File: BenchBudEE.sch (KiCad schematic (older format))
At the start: 0 parts

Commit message: Finished Thermocouple Unit
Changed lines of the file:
@@
 Sheet 1 8
 Title ""
-Date "1 feb 2014"
+Date "4 feb 2014"
 Rev ""
 Comp ""
@@
 $EndDescr
 $Sheet
-S 1450 4800 2400 1650
+S 1450 4800 1700 2600
 U 52ED0B6E
 F0 "Arduino" 50
 F1 "Arduino.sch" 50
+F2 "RELAY+" O R 3150 6750 60
+F3 "RELAY -" I R 3150 6950 60
+F4 "MOSI" O R 3150 6000 60
+F5 "MISO" I R 3150 6150 60
+F6 "SCLK" O R 3150 6300 60
+F7 "CS_N" O R 3150 6450 60
+F8 "LED_EN" O R 3150 5600 60
+F9 "LED_FREQ" O R 3150 5750 60
+F10 "FAN_EN" O R 3150 5200 60
+F11 "TACH_MEAS" I R 3150 5400 60
 $EndSheet
 $Sheet
@@
 F2 "TC IN +" I R 10100 4550 60
 F3 "TC IN -" I R 10100 4800 60
+F4 "MOSI" I L 8000 4550 60
+F5 "MISO" O L 8000 4750 60
+F6 "CLK" I L 8000 4950 60
+F7 "CS_N" I L 8000 5100 60
 $EndSheet
 $Sheet
@@
 F0 "Relay" 50
 F1 "Relay.sch" 50
+F2 "DIN+" I L 7950 6250 60
+F3 "DIN-" O L 7950 6500 60
+F4 "RELAY+" I R 10150 6250 60
+F5 "RELAY-" O R 10150 6550 60
 $EndSheet
 $Sheet
@@
 F0 "LED_Driver" 50
 F1 "LED_Driver.sch" 50
-$EndSheet
-$Sheet
-S 8100 900  1800 1250
-U 52ED0CE0
-F0 "Fan" 50
-F1 "Fan.sch" 50
+F2 "EN" I L 8100 2900 60
+F3 "FREQ" I L 8100 3200 60
+F4 "STRING+" O R 9950 2900 60
+F5 "STRING-" I R 9950 3250 60
 $EndSheet
 $Sheet
@@
 F1 "TerminalBlock.sch" 50
 $EndSheet
+$Sheet
+S 8100 900  1800 1250
+U 52ED0CE0
+F0 "Fan" 50
+F1 "Fan.sch" 50
+F2 "Power+" O R 9900 1200 60
+F3 "Power-" I R 9900 1400 60
+F4 "Tach" I R 9900 1600 60
+F5 "Tach_out" O L 8100 1400 60
+F6 "Fan_in" I L 8100 1200 60
+$EndSheet
 $EndSCHEMATC

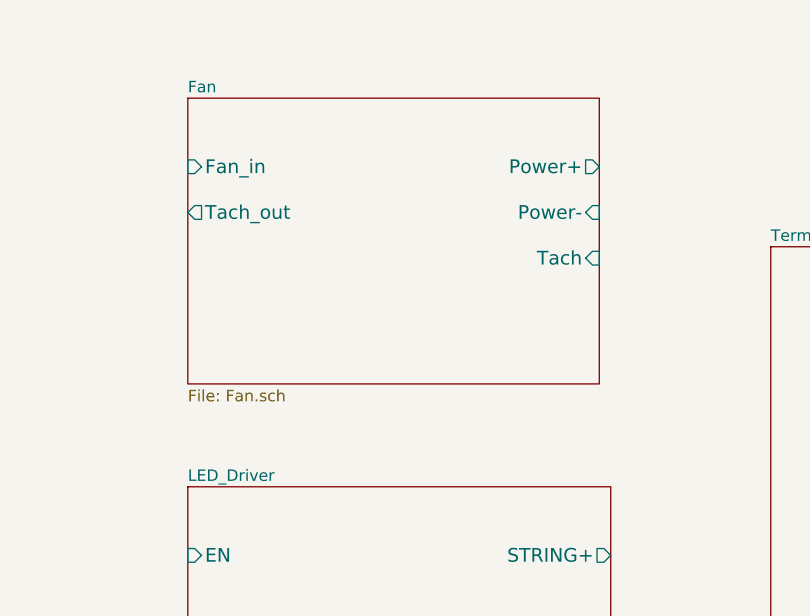
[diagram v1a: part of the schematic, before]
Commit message: After Current/Fan Driver Module
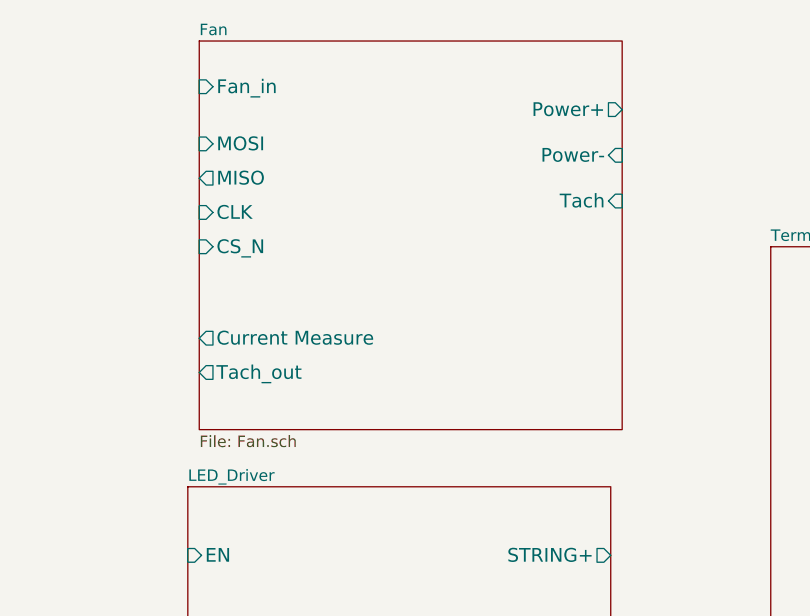
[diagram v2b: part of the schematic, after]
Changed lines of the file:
@@
 $EndSheet
 $Sheet
-S 8100 900  1800 1250
+S 8150 650  1850 1700
 U 52ED0CE0
 F0 "Fan" 50
 F1 "Fan.sch" 50
-F2 "Power+" O R 9900 1200 60
-F3 "Power-" I R 9900 1400 60
-F4 "Tach" I R 9900 1600 60
-F5 "Tach_out" O L 8100 1400 60
-F6 "Fan_in" I L 8100 1200 60
+F2 "Power+" O R 10000 950 60
+F3 "Power-" I R 10000 1150 60
+F4 "Tach" I R 10000 1350 60
+F5 "Tach_out" O L 8150 2100 60
+F6 "Fan_in" I L 8150 850 60
+F7 "Current Measure" O L 8150 1950 60
+F8 "MOSI" I L 8150 1100 60
+F9 "MISO" O L 8150 1250 60
+F10 "CLK" I L 8150 1400 60
+F11 "CS_N" I L 8150 1550 60
 $EndSheet
 $EndSCHEMATC

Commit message: Finished Week 3, Unit 6: Understanding The Power Protection And Filtering Module
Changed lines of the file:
@@
 LIBS:contrib
 LIBS:valves
+LIBS:BenchBudEE
 LIBS:BenchBudEE-cache
 EELAYER 27 0
@@
 $Descr A4 11693 8268
 encoding utf-8
-Sheet 1 8
+Sheet 1 9
 Title ""
-Date "4 feb 2014"
+Date "5 feb 2014"
 Rev ""
 Comp ""
@@
 F11 "CS_N" I L 8150 1550 60
 $EndSheet
+$Sheet
+S 4200 1200 2050 1450
+U 52F22A27
+F0 "PowerAdjustmentMonitor" 50
+F1 "PowerAdjustmentMonitor.sch" 50
+$EndSheet
 $EndSCHEMATC

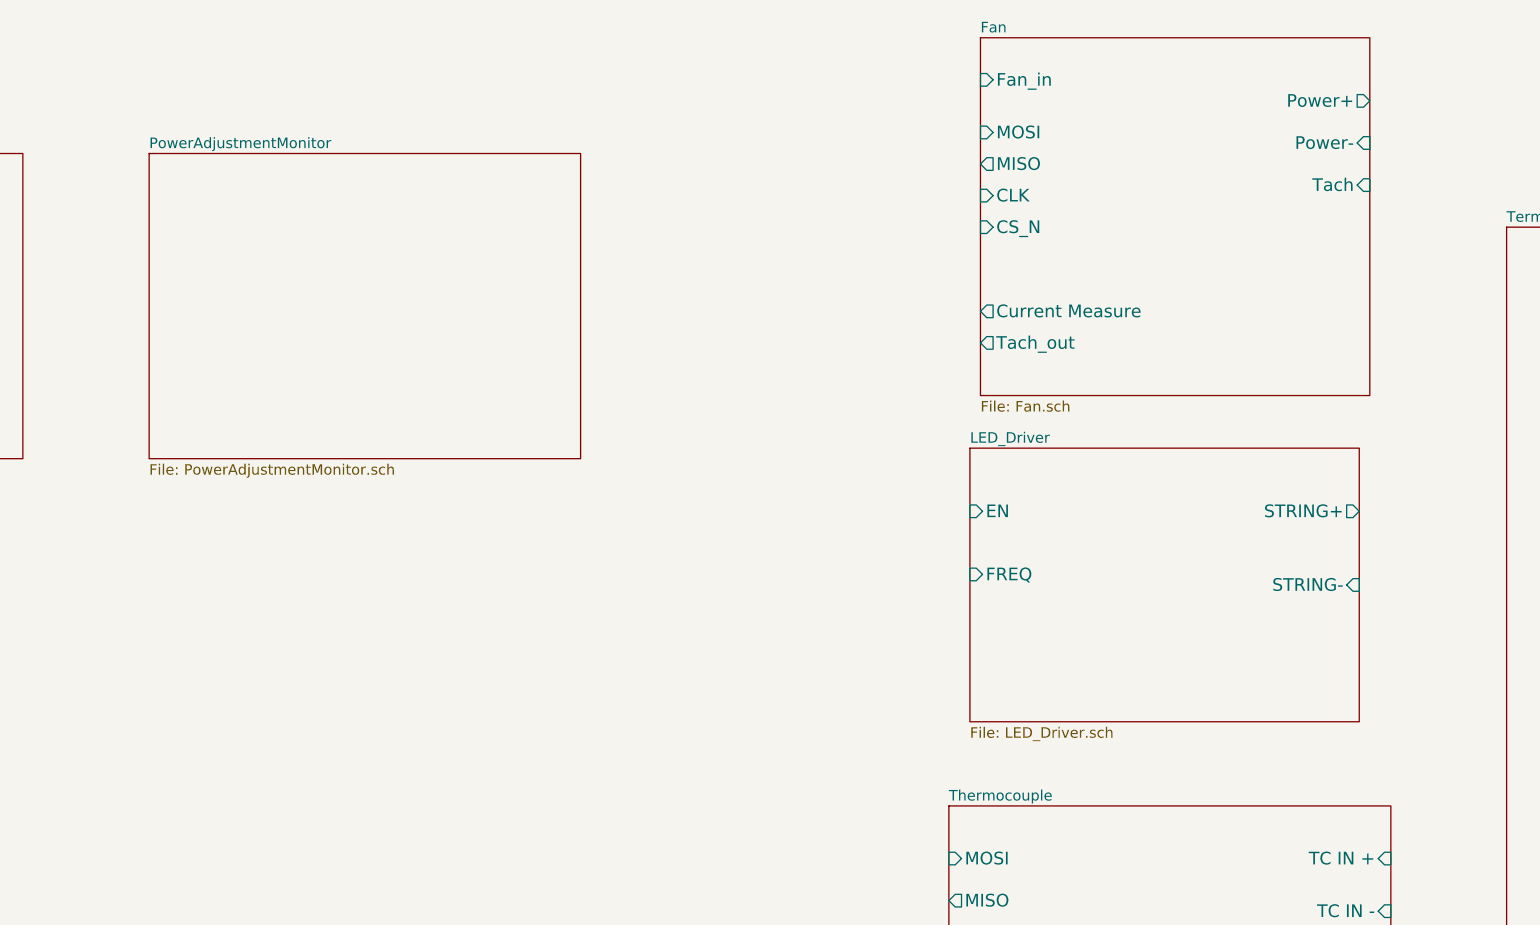
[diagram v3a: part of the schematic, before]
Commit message: Finished Week 3, Unit 7: Power Monitoring Blocks
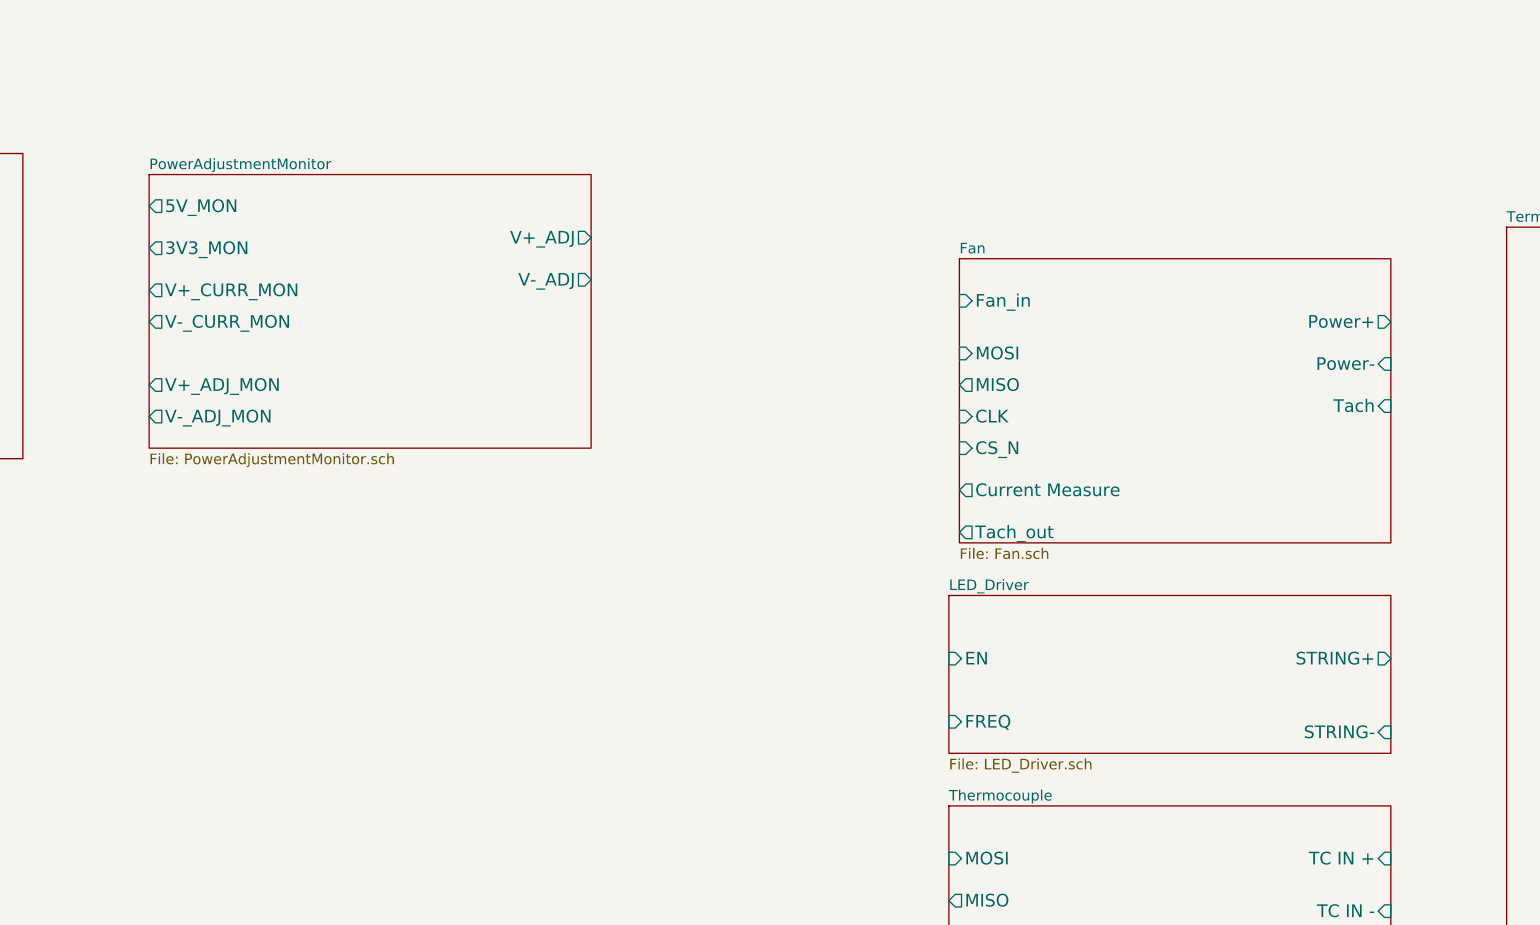
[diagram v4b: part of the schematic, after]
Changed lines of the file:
@@
 Sheet 1 9
 Title ""
-Date "5 feb 2014"
+Date "6 feb 2014"
 Rev ""
 Comp ""
@@
 $EndSheet
 $Sheet
-S 8100 2600 1850 1300
+S 8000 3300 2100 750
 U 52ED0CB4
 F0 "LED_Driver" 50
 F1 "LED_Driver.sch" 50
-F2 "EN" I L 8100 2900 60
-F3 "FREQ" I L 8100 3200 60
-F4 "STRING+" O R 9950 2900 60
-F5 "STRING-" I R 9950 3250 60
+F2 "EN" I L 8000 3600 60
+F3 "FREQ" I L 8000 3900 60
+F4 "STRING+" O R 10100 3600 60
+F5 "STRING-" I R 10100 3950 60
 $EndSheet
 $Sheet
@@
 $EndSheet
 $Sheet
-S 8150 650  1850 1700
+S 8050 1700 2050 1350
 U 52ED0CE0
 F0 "Fan" 50
 F1 "Fan.sch" 50
-F2 "Power+" O R 10000 950 60
-F3 "Power-" I R 10000 1150 60
-F4 "Tach" I R 10000 1350 60
-F5 "Tach_out" O L 8150 2100 60
-F6 "Fan_in" I L 8150 850 60
-F7 "Current Measure" O L 8150 1950 60
-F8 "MOSI" I L 8150 1100 60
-F9 "MISO" O L 8150 1250 60
-F10 "CLK" I L 8150 1400 60
-F11 "CS_N" I L 8150 1550 60
+F2 "Power+" O R 10100 2000 60
+F3 "Power-" I R 10100 2200 60
+F4 "Tach" I R 10100 2400 60
+F5 "Tach_out" O L 8050 3000 60
+F6 "Fan_in" I L 8050 1900 60
+F7 "Current Measure" O L 8050 2800 60
+F8 "MOSI" I L 8050 2150 60
+F9 "MISO" O L 8050 2300 60
+F10 "CLK" I L 8050 2450 60
+F11 "CS_N" I L 8050 2600 60
 $EndSheet
 $Sheet
-S 4200 1200 2050 1450
+S 4200 1300 2100 1300
 U 52F22A27
 F0 "PowerAdjustmentMonitor" 50
 F1 "PowerAdjustmentMonitor.sch" 50
+F2 "V+_ADJ" O R 6300 1600 60
+F3 "V-_ADJ" O R 6300 1800 60
+F4 "3V3_MON" O L 4200 1650 60
+F5 "5V_MON" O L 4200 1450 60
+F6 "V+_ADJ_MON" O L 4200 2300 60
+F7 "V-_ADJ_MON" O L 4200 2450 60
+F8 "V+_CURR_MON" O L 4200 1850 60
+F9 "V-_CURR_MON" O L 4200 2000 60
 $EndSheet
 $EndSCHEMATC

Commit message: Finished Week 3, Unit 10: Revisiting The Current Fan Module
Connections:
- wire segments 0 -> 57
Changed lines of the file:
@@
 LIBS:valves
 LIBS:BenchBudEE
+LIBS:arduino_shieldsNCL
 LIBS:BenchBudEE-cache
 EELAYER 27 0
@@
 Sheet 1 9
 Title ""
-Date "6 feb 2014"
+Date "7 feb 2014"
 Rev ""
 Comp ""
@@
 $EndDescr
 $Sheet
-S 1450 4800 1700 2600
+S 8000 2950 2100 1300
+U 52ED0C08
+F0 "Thermocouple" 50
+F1 "Thermocouple.sch" 50
+F2 "TC IN +" I R 10100 3200 60
+F3 "TC IN -" I R 10100 3450 60
+F4 "MOSI" I L 8000 3200 60
+F5 "MISO" O L 8000 3400 60
+F6 "CLK" I L 8000 3550 60
+F7 "CS_N" I L 8000 3700 60
+$EndSheet
+$Sheet
+S 7900 5350 2200 1000
+U 52ED0C34
+F0 "Relay" 50
+F1 "Relay.sch" 50
+F2 "RELAY_NC" B R 10100 5750 60
+F3 "RELAY_NO" B R 10100 5950 60
+F4 "RELAY_COM" B R 10100 5550 60
+F5 "RELAY+" I L 7900 5650 60
+F6 "RELAY-" O L 7900 5950 60
+$EndSheet
+$Sheet
+S 1200 1150 1950 1450
+U 52ED0C78
+F0 "Power" 50
+F1 "Power.sch" 50
+$EndSheet
+$Sheet
+S 8000 4450 2100 750
+U 52ED0CB4
+F0 "LED_Driver" 50
+F1 "LED_Driver.sch" 50
+F2 "LED_EN_PWM" I L 8000 4700 60
+F3 "LED_STRING+" O R 10100 4650 60
+F4 "LED_STRING-" O R 10100 4900 60
+$EndSheet
+$Sheet
+S 10300 950  850  5400
+U 52ED0D18
+F0 "TerminalBlock" 50
+F1 "TerminalBlock.sch" 50
+F2 "V+_ADJ" I L 10300 1250 60
+F3 "V-_ADJ" I L 10300 1400 60
+F4 "FAN_OUT+" O L 10300 1700 60
+F5 "FAN_OUT-" O L 10300 1900 60
+F6 "TACH_IN" I L 10300 2150 60
+F7 "LED_STRING+" O L 10300 4650 60
+F8 "LED_STRING-" O L 10300 4900 60
+F9 "TC_IN+" I L 10300 3200 60
+F10 "TC_IN-" I L 10300 3450 60
+F11 "RELAY_COM" B L 10300 5550 60
+F12 "RELAY_NO" B L 10300 5950 60
+F13 "RELAY_NC" B L 10300 5750 60
+$EndSheet
+$Sheet
+S 4050 800  2100 1300
+U 52F22A27
+F0 "PowerAdjustmentMonitor" 50
+F1 "PowerAdjustmentMonitor.sch" 50
+F2 "V+_ADJ" O R 6150 1150 60
+F3 "V-_ADJ" O R 6150 1300 60
+F4 "3V3_MON" O L 4050 1150 60
+F5 "5V_MON" O L 4050 950 60
+F6 "V+_ADJ_MON" O L 4050 1800 60
+F7 "V-_ADJ_MON" O L 4050 1950 60
+F8 "V+_CURR_MON" O L 4050 1350 60
+F9 "V-_CURR_MON" O L 4050 1500 60
+$EndSheet
+Wire Wire Line
+	6450 1200 9850 1200
+Wire Wire Line
+	6450 1350 9850 1350
+Wire Wire Line
+	10100 1700 10300 1700
+Wire Wire Line
+	10100 1900 10300 1900
+Wire Wire Line
+	10100 2150 10300 2150
+Wire Wire Line
+	10100 5550 10300 5550
+Wire Wire Line
+	10100 5750 10300 5750
+Wire Wire Line
+	10100 5950 10300 5950
+Wire Wire Line
+	3900 4850 2700 4850
+Wire Wire Line
+	3900 1800 3900 4850
+Wire Wire Line
+	3900 1800 4050 1800
+Wire Wire Line
+	2700 5000 3950 5000
+Wire Wire Line
+	10150 3200 10300 3200
+Wire Wire Line
+	10100 3450 10300 3450
+Wire Wire Line
+	10100 4650 10300 4650
+Wire Wire Line
+	10100 4900 10300 4900
+$Sheet
+S 1000 4700 1700 2600
 U 52ED0B6E
 F0 "Arduino" 50
 F1 "Arduino.sch" 50
-F2 "RELAY+" O R 3150 6750 60
-F3 "RELAY -" I R 3150 6950 60
-F4 "MOSI" O R 3150 6000 60
-F5 "MISO" I R 3150 6150 60
-F6 "SCLK" O R 3150 6300 60
-F7 "CS_N" O R 3150 6450 60
-F8 "LED_EN" O R 3150 5600 60
-F9 "LED_FREQ" O R 3150 5750 60
-F10 "FAN_EN" O R 3150 5200 60
-F11 "TACH_MEAS" I R 3150 5400 60
-$EndSheet
-$Sheet
-S 8000 4300 2100 1300
-U 52ED0C08
-F0 "Thermocouple" 50
-F1 "Thermocouple.sch" 50
-F2 "TC IN +" I R 10100 4550 60
-F3 "TC IN -" I R 10100 4800 60
-F4 "MOSI" I L 8000 4550 60
-F5 "MISO" O L 8000 4750 60
-F6 "CLK" I L 8000 4950 60
-F7 "CS_N" I L 8000 5100 60
-$EndSheet
-$Sheet
-S 7950 6000 2200 1000
-U 52ED0C34
-F0 "Relay" 50
-F1 "Relay.sch" 50
-F2 "DIN+" I L 7950 6250 60
-F3 "DIN-" O L 7950 6500 60
-F4 "RELAY+" I R 10150 6250 60
-F5 "RELAY-" O R 10150 6550 60
-$EndSheet
-$Sheet
-S 1650 1200 1950 1450
-U 52ED0C78
-F0 "Power" 50
-F1 "Power.sch" 50
-$EndSheet
-$Sheet
-S 8000 3300 2100 750
-U 52ED0CB4
-F0 "LED_Driver" 50
-F1 "LED_Driver.sch" 50
-F2 "EN" I L 8000 3600 60
-F3 "FREQ" I L 8000 3900 60
-F4 "STRING+" O R 10100 3600 60
-F5 "STRING-" I R 10100 3950 60
-$EndSheet
-$Sheet
-S 10650 1550 500  5100
-U 52ED0D18
-F0 "TerminalBlock" 50
-F1 "TerminalBlock.sch" 50
-$EndSheet
-$Sheet
-S 8050 1700 2050 1350
+F2 "RELAY+" O R 2700 6900 60
+F3 "MOSI" O R 2700 5400 60
+F4 "MISO" I R 2700 5550 60
+F5 "SCLK" O R 2700 5700 60
+F6 "TACH_MEAS" I R 2700 6100 60
+F7 "RELAY-" O R 2700 7150 60
+F8 "CURR_MEAS" I R 2700 6250 60
+F9 "V+_ADJ_MON" I R 2700 4850 60
+F10 "V-_ADJ_MON" I R 2700 5000 60
+F11 "LED_EN_PWM" O R 2700 6700 60
+F12 "DAC_CS_N" O R 2700 5850 60
+F13 "ADC_CS_N" O R 2700 6450 60
+F14 "FAN_PWM" O R 2700 5250 60
+F15 "FAN_MODE" I R 2700 5150 60
+$EndSheet
+Wire Wire Line
+	2700 5250 6550 5250
+Wire Wire Line
+	6550 5250 6550 1600
+Wire Wire Line
+	6550 1600 8050 1600
+Wire Wire Line
+	6650 5400 2700 5400
+Wire Wire Line
+	6650 1750 6650 5400
+Wire Wire Line
+	6650 1750 8050 1750
+Wire Wire Line
+	6800 5550 2700 5550
+Wire Wire Line
+	6800 1900 6800 5550
+Wire Wire Line
+	6800 1900 8050 1900
+Wire Wire Line
+	6950 5700 2700 5700
+Wire Wire Line
+	6950 2050 6950 5700
+Wire Wire Line
+	6950 2050 8050 2050
+Wire Wire Line
+	2700 5850 7100 5850
+Wire Wire Line
+	7100 5850 7100 2200
+Wire Wire Line
+	7100 2200 8050 2200
+Wire Wire Line
+	8000 3200 6650 3200
+Connection ~ 6650 3200
+Wire Wire Line
+	8000 3400 6800 3400
+Connection ~ 6800 3400
+Wire Wire Line
+	8000 3550 6950 3550
+Connection ~ 6950 3550
+Wire Wire Line
+	2700 6100 7250 6100
+Wire Wire Line
+	7250 6100 7250 2550
+Wire Wire Line
+	7250 2550 8050 2550
+Wire Wire Line
+	2700 6250 7400 6250
+Wire Wire Line
+	7400 6250 7400 2700
+Wire Wire Line
+	7400 2700 8050 2700
+Wire Wire Line
+	2700 6450 7500 6450
+Wire Wire Line
+	7500 6450 7500 3700
+Wire Wire Line
+	7500 3700 8000 3700
+Wire Wire Line
+	2700 6700 7600 6700
+Wire Wire Line
+	7600 6700 7600 4700
+Wire Wire Line
+	7600 4700 8000 4700
+Wire Wire Line
+	2700 6900 7700 6900
+Wire Wire Line
+	7700 6900 7700 5650
+Wire Wire Line
+	7700 5650 7900 5650
+Wire Wire Line
+	2700 7150 7800 7150
+Wire Wire Line
+	7800 7150 7800 5950
+Wire Wire Line
+	7800 5950 7900 5950
+Wire Wire Line
+	3950 5000 3950 1950
+Wire Wire Line
+	3950 1950 4050 1950
+$Sheet
+S 8050 1450 2050 1350
 U 52ED0CE0
 F0 "Fan" 50
 F1 "Fan.sch" 50
-F2 "Power+" O R 10100 2000 60
-F3 "Power-" I R 10100 2200 60
-F4 "Tach" I R 10100 2400 60
-F5 "Tach_out" O L 8050 3000 60
-F6 "Fan_in" I L 8050 1900 60
-F7 "Current Measure" O L 8050 2800 60
-F8 "MOSI" I L 8050 2150 60
-F9 "MISO" O L 8050 2300 60
-F10 "CLK" I L 8050 2450 60
-F11 "CS_N" I L 8050 2600 60
-$EndSheet
-$Sheet
-S 4200 1300 2100 1300
-U 52F22A27
-F0 "PowerAdjustmentMonitor" 50
-F1 "PowerAdjustmentMonitor.sch" 50
-F2 "V+_ADJ" O R 6300 1600 60
-F3 "V-_ADJ" O R 6300 1800 60
-F4 "3V3_MON" O L 4200 1650 60
-F5 "5V_MON" O L 4200 1450 60
-F6 "V+_ADJ_MON" O L 4200 2300 60
-F7 "V-_ADJ_MON" O L 4200 2450 60
-F8 "V+_CURR_MON" O L 4200 1850 60
-F9 "V-_CURR_MON" O L 4200 2000 60
-$EndSheet
+F2 "MOSI" I L 8050 1750 60
+F3 "MISO" O L 8050 1900 60
+F4 "CLK" I L 8050 2050 60
+F5 "CS_N" I L 8050 2200 60
+F6 "FAN_OUT+" O R 10100 1700 60
+F7 "FAN_OUT-" I R 10100 1900 60
+F8 "TACH_IN" I R 10100 2150 60
+F9 "TACH_MEAS" O L 8050 2550 60
+F10 "CURR_MEAS" O L 8050 2700 60
+F11 "FAN_PWM" I L 8050 1600 60
+F12 "FAN_MODE" O L 8050 1500 60
+$EndSheet
+Wire Wire Line
+	8050 1500 6400 1500
+Wire Wire Line
+	6400 1500 6400 5150
+Wire Wire Line
+	6400 5150 2700 5150
 $EndSCHEMATC
